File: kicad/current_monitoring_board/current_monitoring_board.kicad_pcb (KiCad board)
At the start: 2 copper layers, 100.7 x 57.4 mm, 45 parts, among them J1 USB_C_Receptacle_USB2.0_16P, J2 CUI_PD-30, J4 Microsemi_FlashPro-JTAG-10, J5 1702473, J6 1702473, Q1 S8050, Q2 S8050, U1 OPA2333xxD, U2 USBLC6-2P6, U3 AP2112K-3.3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

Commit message: wip
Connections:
- RLe1 pad 1: Net-(U1A--) -> V_ref
- RLo1 pad 1: Net-(U1B--) -> V_ref
- U1 pad 1: Net-(U1A--) -> V_ref
- U1 pad 2: Net-(U1A--) -> V_ref
- U1 pad 6: Net-(U1B--) -> V_ref
- U1 pad 7: Net-(U1B--) -> V_ref
- U6 pad 8: unconnected-(U6-IO32-Pad8) -> V_ref
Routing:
- net V_ref: track 0.00 -> 59.5 mm, vias 0 -> 6
- net Net-(U1A--): track 19.7 -> 0.00 mm, vias 4 -> 0
- net Net-(U1B--): track 7.86 -> 0.00 mm
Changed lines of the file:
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@@
 			(size 1.5 0.9)
 			(layers "F.Cu" "F.Mask" "F.Paste")
-			(net "unconnected-(U6-IO32-Pad8)")
+			(net "V_ref")
 			(pinfunction "IO32_8")
 			(pintype "bidirectional")
@@
 			(layers "F.Cu" "F.Mask" "F.Paste")
 			(roundrect_rratio 0.25)
-			(net "Net-(U1A--)")
+			(net "V_ref")
 			(pintype "output")
 		)
@@
 			(layers "F.Cu" "F.Mask" "F.Paste")
 			(roundrect_rratio 0.25)
-			(net "Net-(U1A--)")
+			(net "V_ref")
 			(pinfunction "-_2")
 			(pintype "input")
@@
 			(layers "F.Cu" "F.Mask" "F.Paste")
 			(roundrect_rratio 0.25)
-			(net "Net-(U1B--)")
+			(net "V_ref")
 			(pinfunction "-_6")
 			(pintype "input")
@@
 			(layers "F.Cu" "F.Mask" "F.Paste")
 			(roundrect_rratio 0.25)
-			(net "Net-(U1B--)")
+			(net "V_ref")
 			(pintype "output")
 		)
@@
 			(layers "F.Cu" "F.Mask" "F.Paste")
 			(roundrect_rratio 0.243902)
-			(net "Net-(U1B--)")
+			(net "V_ref")
 			(pintype "passive")
 		)
@@
 			(layers "F.Cu" "F.Mask" "F.Paste")
 			(roundrect_rratio 0.243902)
-			(net "Net-(U1A--)")
+			(net "V_ref")
 			(pintype "passive")
 		)
@@
 	)
 	(segment
-		(start 100.1325 105.075)
-		(end 100.1325 106.5175)
-		(width 0.2)
-		(layer "F.Cu")
-		(net "Net-(U1A--)")
-	)
-	(segment
-		(start 97.325 107.325)
-		(end 94.325 104.325)
-		(width 0.2)
-		(layer "F.Cu")
-		(net "Net-(U1A--)")
-	)
-	(segment
-		(start 94.825 97.325)
-		(end 95.325 97.325)
-		(width 0.2)
-		(layer "F.Cu")
-		(net "Net-(U1A--)")
-	)
-	(segment
-		(start 95.325 97.325)
-		(end 96.3625 98.3625)
-		(width 0.2)
-		(layer "F.Cu")
-		(net "Net-(U1A--)")
-	)
-	(segment
-		(start 94.325 104.325)
-		(end 94.325 101.825)
-		(width 0.2)
-		(layer "F.Cu")
-		(net "Net-(U1A--)")
-	)
-	(segment
-		(start 100.1325 105.075)
-		(end 101.4025 105.075)
-		(width 0.2)
-		(layer "F.Cu")
-		(net "Net-(U1A--)")
-	)
-	(segment
-		(start 96.3625 98.3625)
-		(end 96.3625 98.75)
-		(width 0.2)
-		(layer "F.Cu")
-		(net "Net-(U1A--)")
-	)
-	(segment
-		(start 100.1325 106.5175)
-		(end 99.825 106.825)
-		(width 0.2)
-		(layer "F.Cu")
-		(net "Net-(U1A--)")
-	)
-	(via
-		(at 99.825 106.825)
-		(size 0.6)
-		(drill 0.3)
-		(layers "F.Cu" "B.Cu")
-		(net "Net-(U1A--)")
-	)
-	(via
-		(at 97.325 107.325)
-		(size 0.6)
-		(drill 0.3)
-		(layers "F.Cu" "B.Cu")
-		(net "Net-(U1A--)")
-	)
-	(via
-		(at 94.825 97.325)
-		(size 0.6)
-		(drill 0.3)
-		(layers "F.Cu" "B.Cu")
-		(net "Net-(U1A--)")
-	)
-	(via
-		(at 94.325 101.825)
-		(size 0.6)
-		(drill 0.3)
-		(layers "F.Cu" "B.Cu")
-		(net "Net-(U1A--)")
-	)
-	(segment
-		(start 94.325 97.825)
-		(end 94.825 97.325)
-		(width 0.2)
-		(layer "B.Cu")
-		(net "Net-(U1A--)")
-	)
-	(segment
-		(start 99.325 107.325)
-		(end 97.325 107.325)
-		(width 0.2)
-		(layer "B.Cu")
-		(net "Net-(U1A--)")
-	)
-	(segment
-		(start 99.825 106.825)
-		(end 99.325 107.325)
-		(width 0.2)
-		(layer "B.Cu")
-		(net "Net-(U1A--)")
-	)
-	(segment
-		(start 94.325 101.825)
-		(end 94.325 97.825)
-		(width 0.2)
-		(layer "B.Cu")
-		(net "Net-(U1A--)")
-	)
-	(segment
 		(start 96.3625 93.1625)
 		(end 98.1625 93.1625)
@@
 	)
 	(segment
-		(start 98.8625 110.025)
-		(end 100.1325 110.025)
-		(width 0.2)
-		(layer "F.Cu")
-		(net "Net-(U1B--)")
-	)
-	(segment
-		(start 98.8625 113.075)
-		(end 98.8625 110.025)
-		(width 0.2)
-		(layer "F.Cu")
-		(net "Net-(U1B--)")
-	)
-	(segment
-		(start 96.3625 115.575)
-		(end 98.8625 113.075)
-		(width 0.2)
-		(layer "F.Cu")
-		(net "Net-(U1B--)")
-	)
-	(segment
 		(start 140.825 93.825)
 		(end 140.825 93.325)
@@
 		(net "Net-(J1-CC2)")
 	)
+	(segment
+		(start 100.1325 105.075)
+		(end 100.1325 106.5175)
+		(width 0.2)
+		(layer "F.Cu")
+		(net "V_ref")
+	)
+	(segment
+		(start 97.325 107.325)
+		(end 94.325 104.325)
+		(width 0.2)
+		(layer "F.Cu")
+		(net "V_ref")
+	)
+	(segment
+		(start 96.3625 98.75)
+		(end 96.3625 98.6375)
+		(width 0.2)
+		(layer "F.Cu")
+		(net "V_ref")
+	)
+	(segment
+		(start 117.875 85.405)
+		(end 118.825 85.405)
+		(width 0.2)
+		(layer "F.Cu")
+		(net "V_ref")
+	)
+	(segment
+		(start 115.5 87.78)
+		(end 117.875 85.405)
+		(width 0.2)
+		(layer "F.Cu")
+		(net "V_ref")
+	)
+	(segment
+		(start 94.825 97.325)
+		(end 95.325 97.325)
+		(width 0.2)
+		(layer "F.Cu")
+		(net "V_ref")
+	)
+	(segment
+		(start 96.3625 98.6375)
+		(end 98.5 96.5)
+		(width 0.2)
+		(layer "F.Cu")
+		(net "V_ref")
+	)
+	(segment
+		(start 95.325 97.325)
+		(end 96.3625 98.3625)
+		(width 0.2)
+		(layer "F.Cu")
+		(net "V_ref")
+	)
+	(segment
+		(start 94.325 104.325)
+		(end 94.325 101.825)
+		(width 0.2)
+		(layer "F.Cu")
+		(net "V_ref")
+	)
+	(segment
+		(start 100.1325 105.075)
+		(end 101.4025 105.075)
+		(width 0.2)
+		(layer "F.Cu")
+		(net "V_ref")
+	)
+	(segment
+		(start 115.5 94.5)
+		(end 115.5 87.78)
+		(width 0.2)
+		(layer "F.Cu")
+		(net "V_ref")
+	)
+	(segment
+		(start 96.3625 98.3625)
+		(end 96.3625 98.75)
+		(width 0.2)
+		(layer "F.Cu")
+		(net "V_ref")
+	)
+	(segment
+		(start 98.8625 110.025)
+		(end 100.1325 110.025)
+		(width 0.2)
+		(layer "F.Cu")
+		(net "V_ref")
+	)
+	(segment
+		(start 98.8625 113.075)
+		(end 98.8625 110.025)
+		(width 0.2)
+		(layer "F.Cu")
+		(net "V_ref")
+	)
+	(segment
+		(start 96.3625 115.575)
+		(end 98.8625 113.075)
+		(width 0.2)
+		(layer "F.Cu")
+		(net "V_ref")
+	)
+	(segment
+		(start 100.1325 106.5175)
+		(end 99.825 106.825)
+		(width 0.2)
+		(layer "F.Cu")
+		(net "V_ref")
+	)
+	(via
+		(at 115.5 94.5)
+		(size 0.6)
+		(drill 0.3)
+		(layers "F.Cu" "B.Cu")
+		(net "V_ref")
+	)
+	(via
+		(at 99.825 106.825)
+		(size 0.6)
+		(drill 0.3)
+		(layers "F.Cu" "B.Cu")
+		(net "V_ref")
+	)
+	(via
+		(at 98.5 96.5)
+		(size 0.6)
+		(drill 0.3)
+		(layers "F.Cu" "B.Cu")
+		(net "V_ref")
+	)
+	(via
+		(at 97.325 107.325)
+		(size 0.6)
+		(drill 0.3)
+		(layers "F.Cu" "B.Cu")
+		(net "V_ref")
+	)
+	(via
+		(at 94.825 97.325)
+		(size 0.6)
+		(drill 0.3)
+		(layers "F.Cu" "B.Cu")
+		(net "V_ref")
+	)
+	(via
+		(at 94.325 101.825)
+		(size 0.6)
+		(drill 0.3)
+		(layers "F.Cu" "B.Cu")
+		(net "V_ref")
+	)
+	(segment
+		(start 94.325 97.825)
+		(end 94.825 97.325)
+		(width 0.2)
+		(layer "B.Cu")
+		(net "V_ref")
+	)
+	(segment
+		(start 100.5 94.5)
+		(end 115.5 94.5)
+		(width 0.2)
+		(layer "B.Cu")
+		(net "V_ref")
+	)
+	(segment
+		(start 99.325 107.325)
+		(end 97.325 107.325)
+		(width 0.2)
+		(layer "B.Cu")
+		(net "V_ref")
+	)
+	(segment
+		(start 99.825 106.825)
+		(end 99.325 107.325)
+		(width 0.2)
+		(layer "B.Cu")
+		(net "V_ref")
+	)
+	(segment
+		(start 98.5 96.5)
+		(end 100.5 94.5)
+		(width 0.2)
+		(layer "B.Cu")
+		(net "V_ref")
+	)
+	(segment
+		(start 94.325 101.825)
+		(end 94.325 97.825)
+		(width 0.2)
+		(layer "B.Cu")
+		(net "V_ref")
+	)
 	(zone

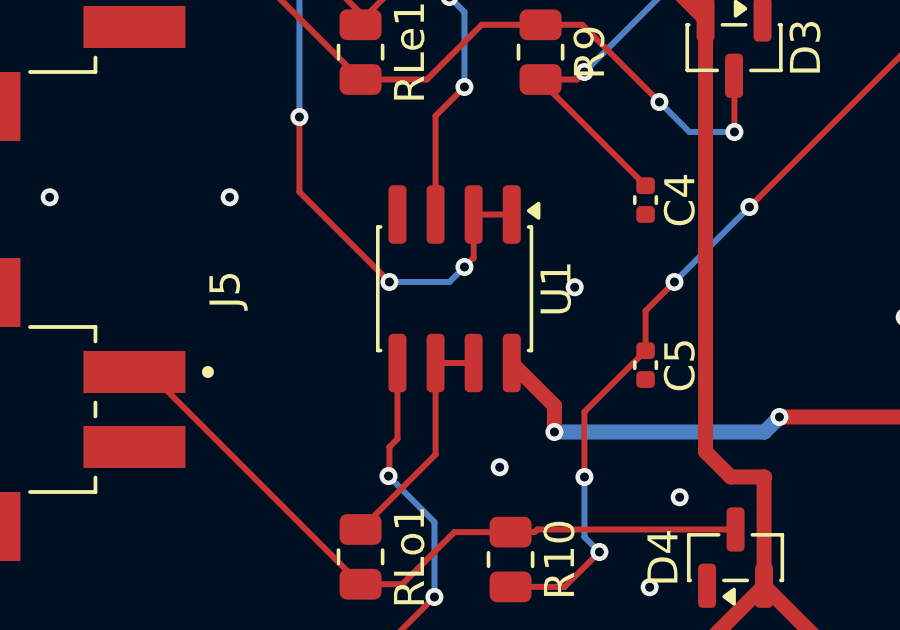
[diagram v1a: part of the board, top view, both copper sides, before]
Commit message: update vref vias
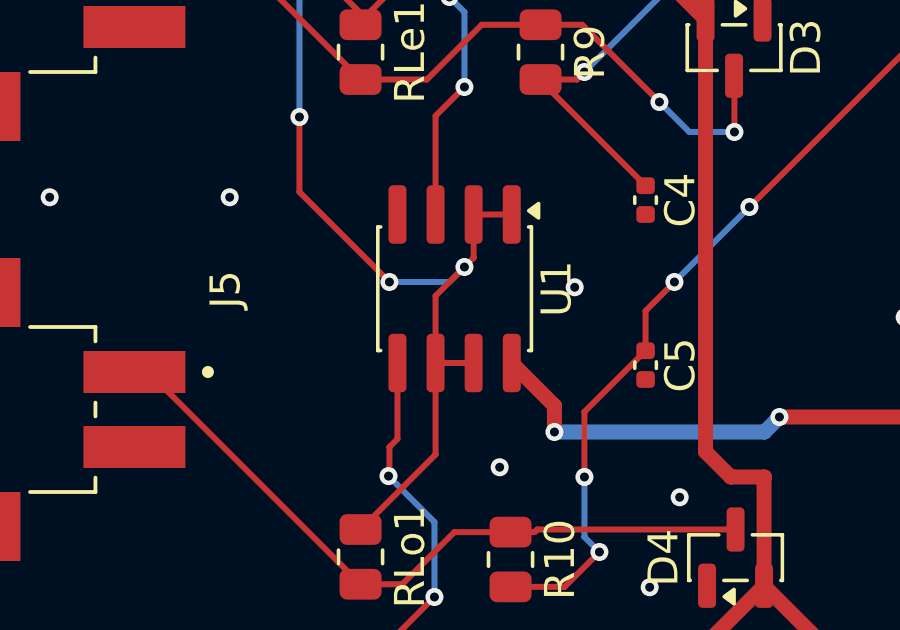
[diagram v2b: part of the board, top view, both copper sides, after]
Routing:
- net V_ref: track 59.5 -> 63.1 mm
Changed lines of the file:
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@@
+	)
+	(segment
+		(start 98.8625 107.7875)
+		(end 99.825 106.825)
+		(width 0.2)
+		(layer "F.Cu")
+		(net "V_ref")
 	)
 	(segment
@@
 		(width 0.2)
 		(layer "F.Cu")
+		(net "V_ref")
+	)
+	(segment
+		(start 98.8625 110.025)
+		(end 98.8625 107.7875)
+		(width 0.2)
+		(layer "F.Cu")
